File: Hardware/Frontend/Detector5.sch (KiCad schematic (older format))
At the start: 27 parts, among them J7 Conn_Coaxial, U13 OPA145ID, U14 OPA145ID, U15 OPA145ID

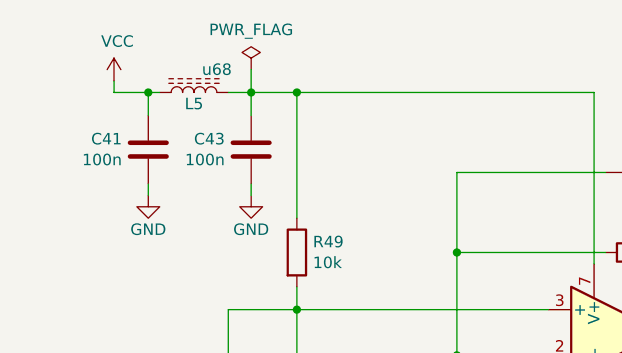
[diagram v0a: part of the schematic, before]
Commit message: add bom
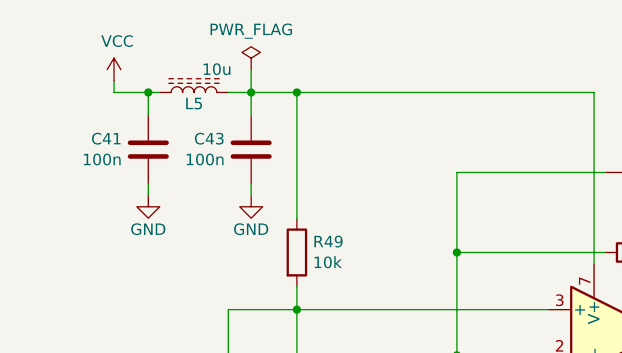
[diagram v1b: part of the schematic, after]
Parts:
- L5: value u68 -> 10u
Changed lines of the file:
@@
 AR Path="/6126CCD1/6143C480" Ref="L5"  Part="1"
 F 0 "L5" V 2700 2250 50  0000 C CNN
-F 1 "u68" V 2850 2350 50  0000 C CNN
+F 1 "10u" V 2850 2350 50  0000 C CNN
 F 2 "Inductor_SMD:L_0805_2012Metric" H 2750 2250 50  0001 C CNN
 F 3 "" H 2750 2250 50  0001 C CNN
